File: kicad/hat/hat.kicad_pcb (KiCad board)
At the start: 2 copper layers, 65 x 24 mm, 3 parts, among them J1 GPIO

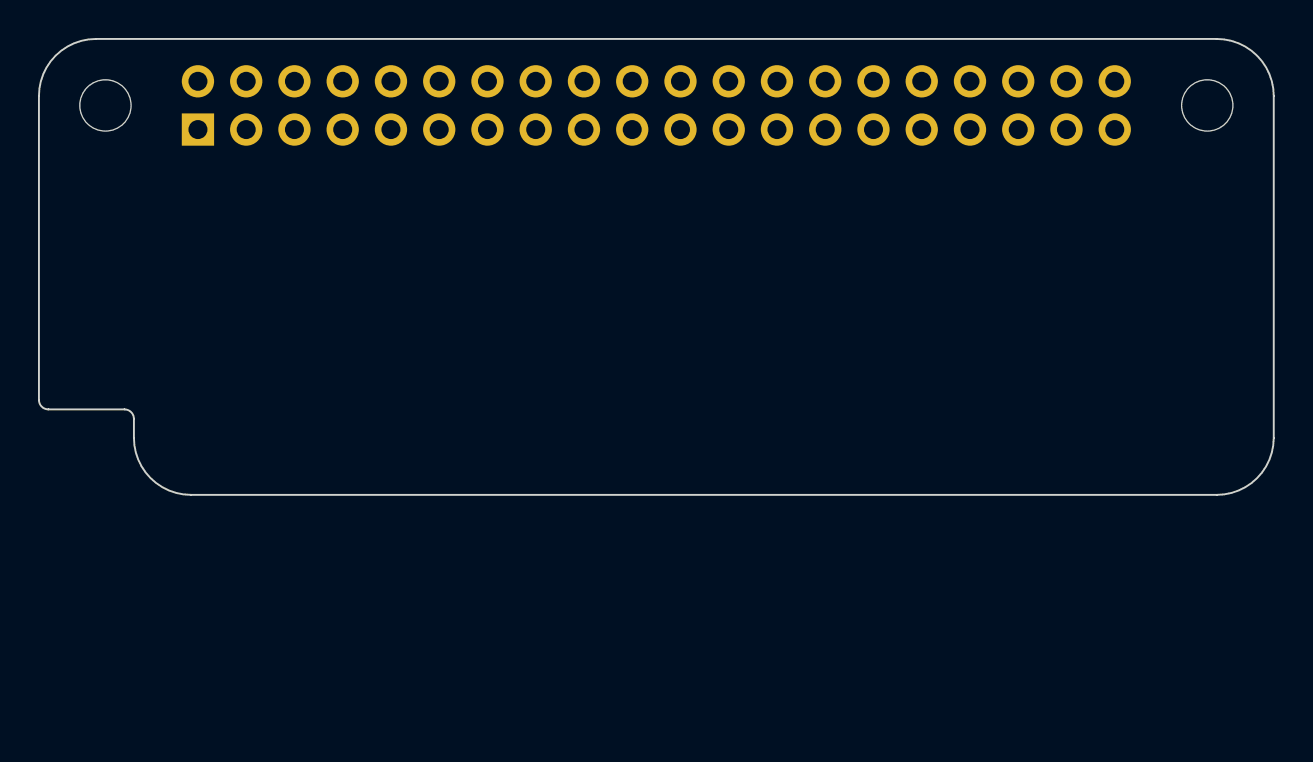
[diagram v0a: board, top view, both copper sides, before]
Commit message: add footprints to hat
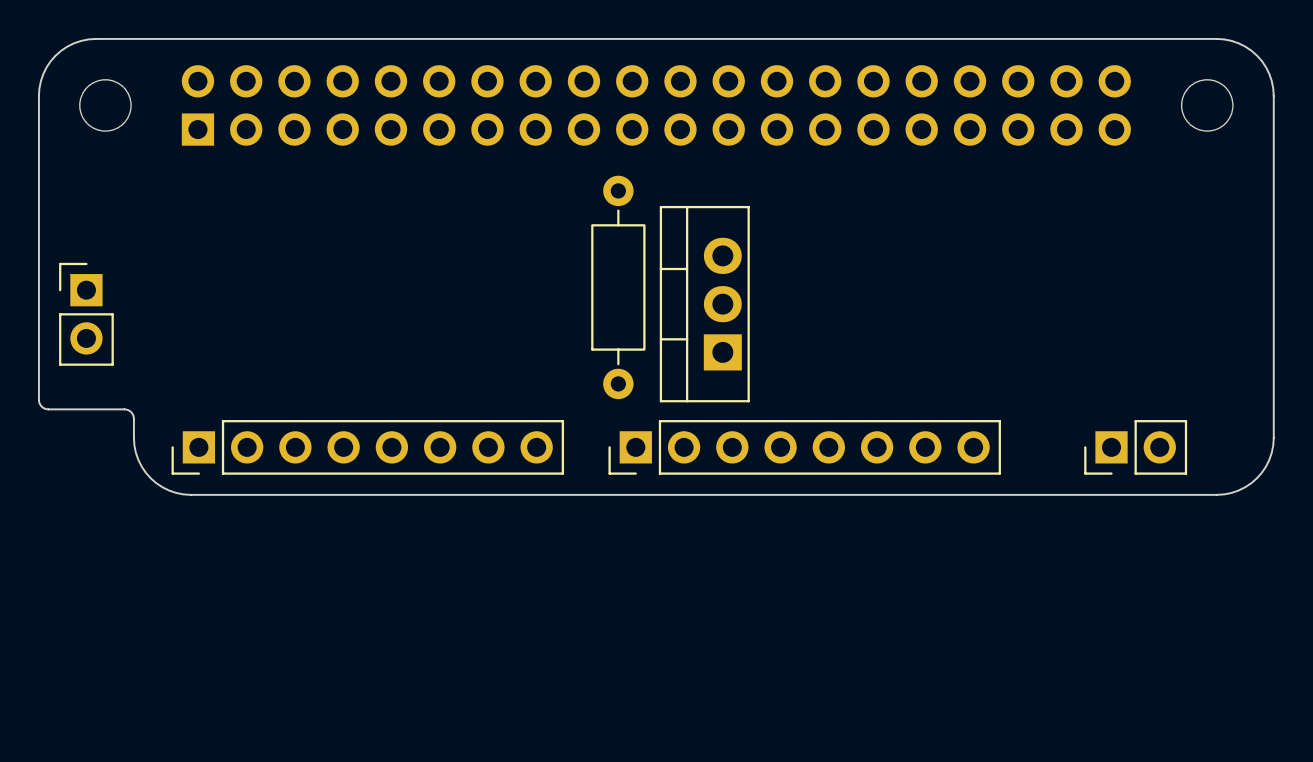
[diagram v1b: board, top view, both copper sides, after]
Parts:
- added DisplayOnOffSwitch1: IRLZ44N, Package_TO_SOT_THT:TO-220-3_Vertical, F.Cu at (136.0, 60.5)
- added J2: FrontButtons, Connector_PinHeader_2.54mm:PinHeader_1x08_P2.54mm_Vertical, F.Cu at (108.4, 65.5)
- added J3: DisplaySPI, Connector_PinHeader_2.54mm:PinHeader_1x08_P2.54mm_Vertical, F.Cu at (131.4, 65.5)
- added J5: PowerButton, Connector_PinHeader_2.54mm:PinHeader_1x02_P2.54mm_Vertical, F.Cu at (102.5, 57.2)
- added J6: PowerWakeup, Connector_PinHeader_2.54mm:PinHeader_1x02_P2.54mm_Vertical, F.Cu at (156.5, 65.5)
- added R1: R, Resistor_THT:R_Axial_DIN0207_L6.3mm_D2.5mm_P10.16mm_Horizontal, F.Cu at (130.5, 62.2)
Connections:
- J1 pad 10: /GPIO15/RXD0 -> /Btn5
- J1 pad 11: /GPIO17 -> /Btn4
- J1 pad 12: /GPIO18/PCM.CLK -> /Btn3
- J1 pad 13: /GPIO27 -> /Btn2
- J1 pad 16: /GPIO23 -> /Btn1
- J1 pad 18: /GPIO24 -> /BtnPower
- J1 pad 22: /GPIO25 -> /DisplayOnOff
- J1 pad 7: /GPIO4/GPCLK0 -> /Btn6

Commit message: WIP
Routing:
- net /BtnPower: track 0.00 -> 90.2 mm
- net +5V: track 0.00 -> 56.9 mm
- net +3V3: track 0.00 -> 31.5 mm
- net /GPIO10/SPI0.MOSI: track 0.00 -> 29.7 mm
- net /GPIO8/SPI0.CE0: track 0.00 -> 27.4 mm
- net /GPIO11/SPI0.SCLK: track 0.00 -> 22.3 mm
- net /GPIO9/SPI0.MISO: track 0.00 -> 21.5 mm
- net /Btn5: track 0.00 -> 20.3 mm
- net /Btn1: track 0.00 -> 20.2 mm
- net /Btn3: track 0.00 -> 20.2 mm
- net /GPIO5: track 0.00 -> 17.9 mm
- net /GPIO6: track 0.00 -> 17.9 mm
- net /Btn6: track 0.00 -> 17.8 mm
- net /Btn4: track 0.00 -> 17.8 mm
- net /Btn2: track 0.00 -> 16.8 mm
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
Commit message: start buttons board
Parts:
- added J6: BetteryLevel, Connector_PinHeader_2.54mm:PinHeader_1x02_P2.54mm_Vertical, F.Cu at (151.5, 65.5)
- J3: footprint Connector_PinHeader_2.54mm:PinHeader_1x08_P2.54mm_Vertical -> Connector_PinHeader_2.00mm:PinHeader_1x08_P2.00mm_Vertical
- moved J6 2.76 mm to (159.2, 65.5)
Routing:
- net /GPIO10/SPI0.MOSI: track 29.7 -> 27.5 mm
- net /BtnPower: track 90.2 -> 91.4 mm
- net /GPIO9/SPI0.MISO: track 21.5 -> 22.6 mm
- net /GPIO5: track 17.9 -> 16.9 mm
- net /GPIO6: track 17.9 -> 17.2 mm
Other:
- board text removed: "PoE"

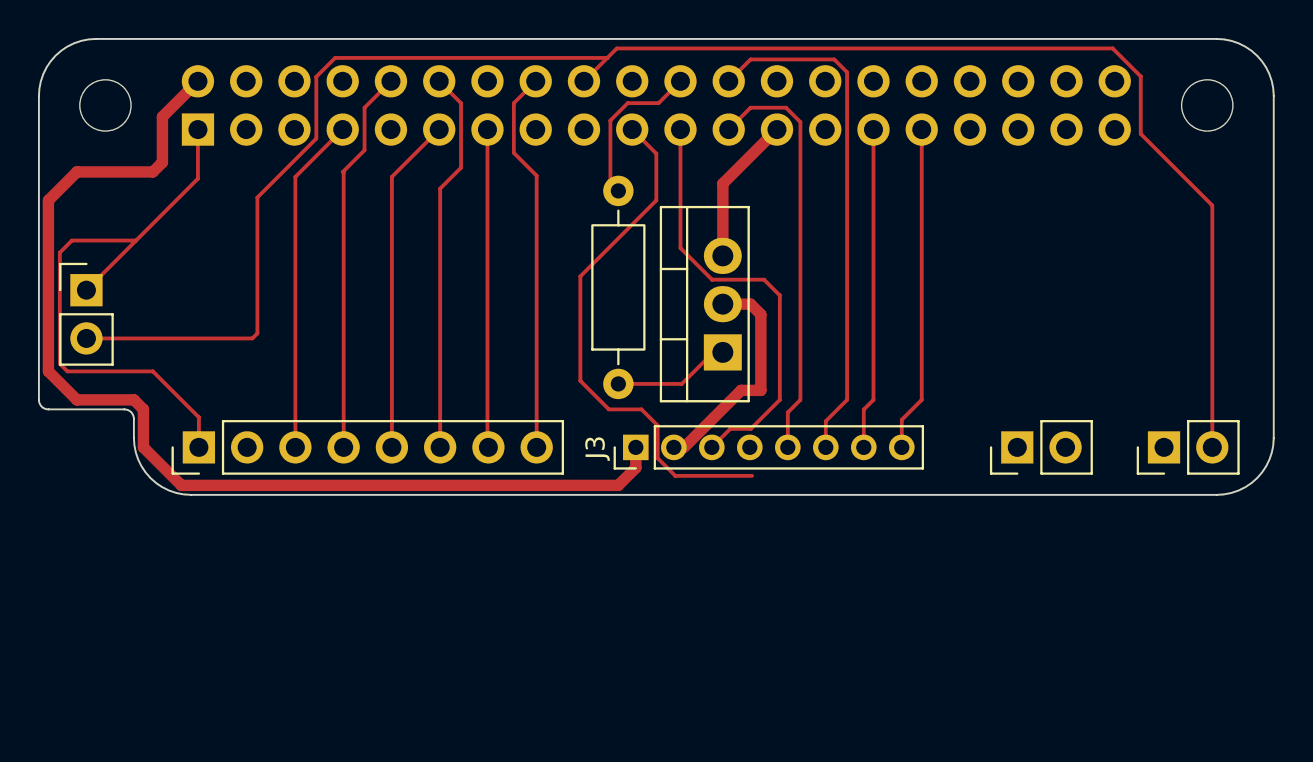
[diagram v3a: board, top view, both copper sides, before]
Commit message: connect adc to battery
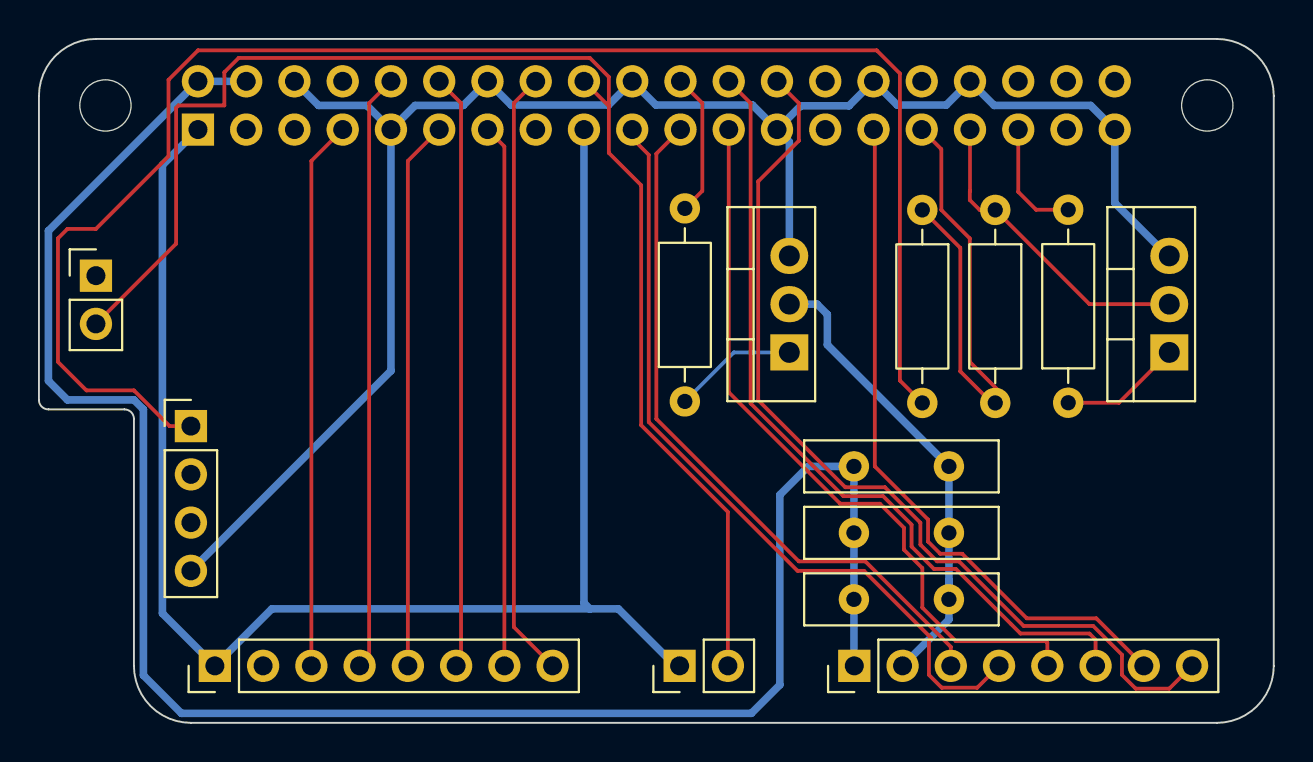
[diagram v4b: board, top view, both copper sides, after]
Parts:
- removed the J6 at (159.2, 65.5)
- added BatteryVoltageDividerOnOffSwitch1: IRLF44N, Package_TO_SOT_THT:TO-220-3_Vertical, F.Cu at (159.5, 60.5)
- added C1: 100nF, Capacitor_THT:C_Disc_D10.0mm_W2.5mm_P5.00mm, F.Cu at (142.9, 73.5)
- added C2: 1uF, Capacitor_THT:C_Disc_D10.0mm_W2.5mm_P5.00mm, F.Cu at (142.9, 70.0)
- added C3: 10uF, Capacitor_THT:C_Disc_D10.0mm_W2.5mm_P5.00mm, F.Cu at (142.9, 66.5)
- added J4: BatteryLevel, Connector_PinHeader_2.54mm:PinHeader_1x04_P2.54mm_Vertical, F.Cu at (108.0, 64.4)
- added R2: R, Resistor_THT:R_Axial_DIN0207_L6.3mm_D2.5mm_P10.16mm_Horizontal, F.Cu at (146.5, 53.0)
- added R3: R, Resistor_THT:R_Axial_DIN0207_L6.3mm_D2.5mm_P10.16mm_Horizontal, F.Cu at (150.3, 53.0)
- added R4: R, Resistor_THT:R_Axial_DIN0207_L6.3mm_D2.5mm_P10.16mm_Horizontal, F.Cu at (154.2, 63.1)
- J3: footprint Connector_PinHeader_2.00mm:PinHeader_1x08_P2.00mm_Vertical -> Connector_PinHeader_2.54mm:PinHeader_1x08_P2.54mm_Vertical
- J6: value BetteryLevel -> PowerWakeup
- moved J6 49.3 mm to (103.0, 56.5), turned to 0 degrees
- moved J5 37.0 mm to (133.7, 77.0), turned to 90 degrees
- moved J3 16.3 mm to (142.9, 77.0)
- moved J2 11.5 mm to (109.3, 77.0)
- moved R1 3.62 mm to (134.0, 63.1)
- moved DisplayOnOffSwitch1 3.50 mm to (139.5, 60.5)
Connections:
- J1 pad 31: /GPIO6 -> /BatterINP16
- J1 pad 33: /GPIO13/PWM1 -> /BatterNNP16
- J1 pad 35: /GPIO19/PCM.FS -> /BatteryVoltageDividerOnOff
- J3 pad 8: /GPIO6 -> /GPIO7/SPI0.CE1
- J6 pad 1: (no net) -> unconnected-(J6-Pin_1-Pad1)
- J6 pad 2: (no net) -> /BtnPower
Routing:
- net GND: track 7.83 -> 92.9 mm
- net /BatteryPwr: track 0.00 -> 84.0 mm
- net +3V3: track 31.5 -> 82.5 mm
- net /GPIO7/SPI0.CE1: track 0.00 -> 49.1 mm
- net +5V: track 56.9 -> 101.2 mm
- net /BatterINP16: track 0.00 -> 28.0 mm
- net /GPIO5: track 16.9 -> 36.9 mm
- net /BtnPower: track 91.4 -> 73.9 mm
- net /GPIO6: track 17.2 -> 0.00 mm
- net /GPIO11/SPI0.SCLK: track 22.0 -> 39.2 mm
- net /BatterNNP16: track 0.00 -> 16.5 mm
- net /GPIO8/SPI0.CE0: track 27.2 -> 42.8 mm
- net /GPIO9/SPI0.MISO: track 22.6 -> 37.2 mm
- net /GPIO10/SPI0.MOSI: track 27.5 -> 41.8 mm
- net /SPI_GND: track 11.5 -> 25.4 mm
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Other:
- board size 65 x 24 mm -> 65 x 36 mm

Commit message: fix hat bugs
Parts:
- J3: footprint Connector_PinHeader_2.54mm:PinHeader_1x08_P2.54mm_Vertical -> Connector_PinHeader_2.00mm:PinHeader_1x08_P2.00mm_Vertical
- R1, R4: value R -> 10k
- R2: value R -> 47k
- R3: value R -> 33k
- moved C1 16.9 mm to (158.0, 66.0), turned to 180 degrees
- moved C3 16.1 mm to (158.0, 72.0), turned to 180 degrees
- moved C2 15.1 mm to (158.0, 69.0), turned to 180 degrees
- moved J3 14.1 mm to (157.0, 77.0), turned to -90 degrees
- moved J4 7.62 mm to (108.0, 72.0), turned to 180 degrees
- moved J6 5.02 mm to (108.0, 56.0)
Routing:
- net +5V: track 101.2 -> 121.3 mm
- net /GPIO9/SPI0.MISO: track 37.2 -> 53.8 mm
- net /GPIO7/SPI0.CE1: track 49.1 -> 33.0 mm
- net /GPIO5: track 36.9 -> 32.1 mm
- net /BtnPower: track 73.9 -> 69.4 mm
- net /GPIO10/SPI0.MOSI: track 41.8 -> 46.0 mm
- net /SPI_GND: track 25.4 -> 29.6 mm
- net /BatteryPwr: track 84.0 -> 80.7 mm
- net GND: track 92.9 -> 89.9 mm
- net +3V3: track 82.5 -> 85.0 mm
- net /GPIO8/SPI0.CE0: track 42.8 -> 40.4 mm
- net /GPIO11/SPI0.SCLK: track 39.2 -> 40.3 mm
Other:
- outline, holes or cut-outs redrawn
